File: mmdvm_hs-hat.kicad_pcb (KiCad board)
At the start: 2 copper layers, 65.1 x 30.2 mm, 82 parts, among them P1 I2C, P2 DISPLAY, P3 SMA, P4 STLINK, SW1 DNI, U1 ADF7021, U2 STM32F103C8T6, X1 TCXO, Y1 8MHz

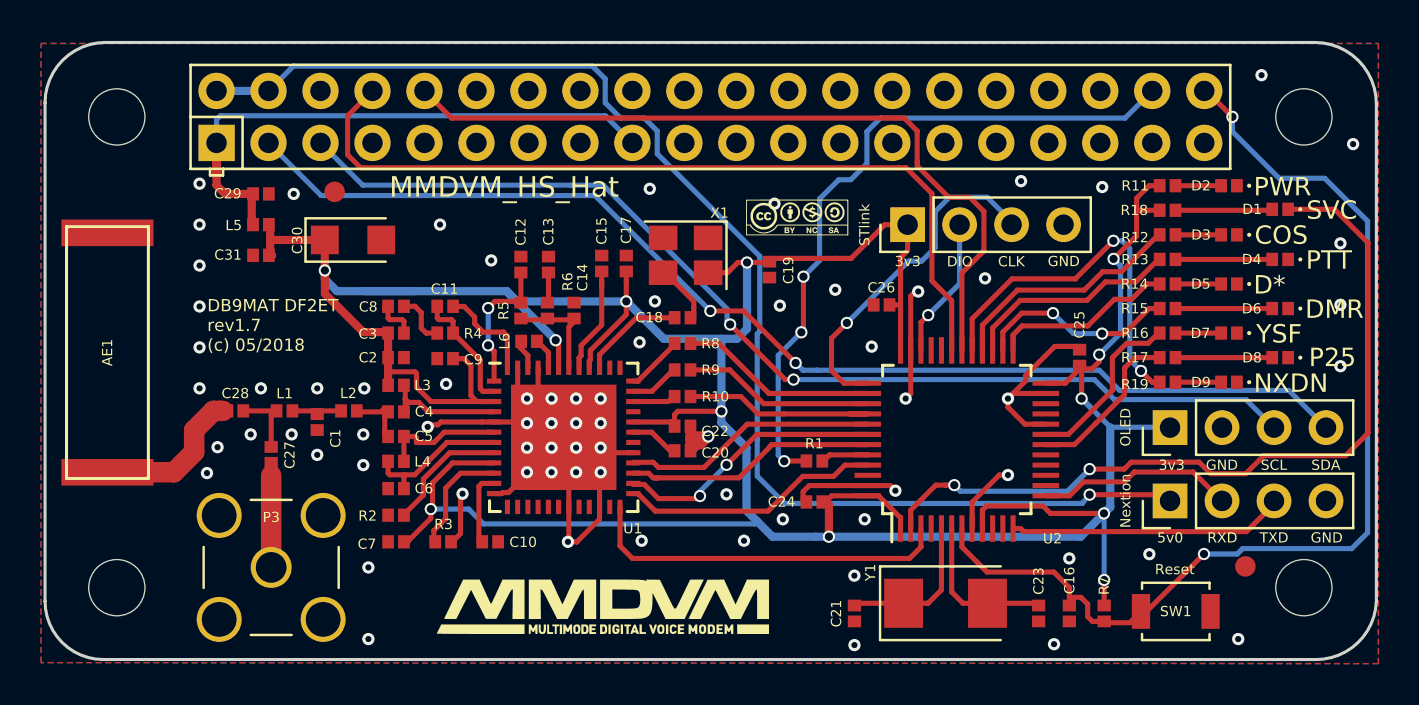
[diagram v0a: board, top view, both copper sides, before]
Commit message: Few track re-routed, few components moved. SMA sligthly moved to get better GND one for corners. Center tracks in 2x20 connector.
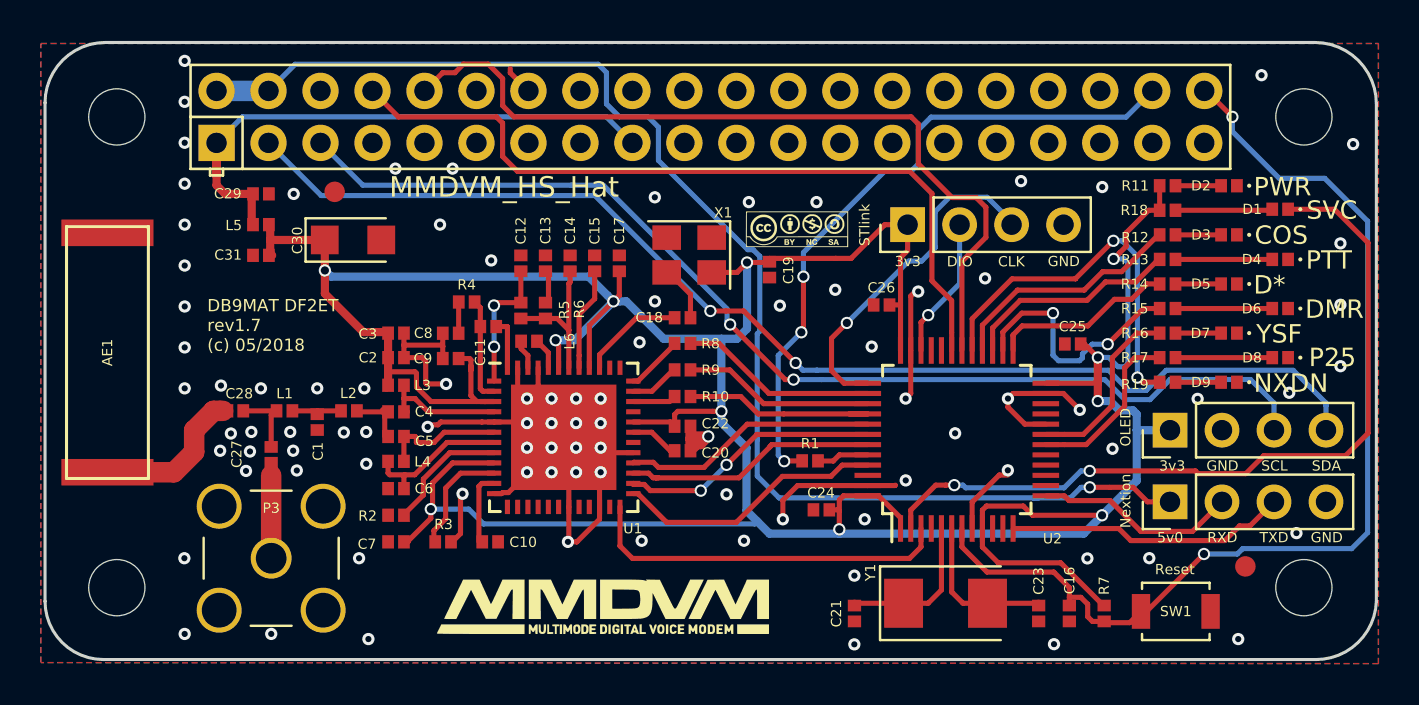
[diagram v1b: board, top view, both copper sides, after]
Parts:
- moved C8 2.98 mm to (175.3, 119.8)
- moved C11 2.33 mm to (177.1, 119.5)
- moved C14 2.32 mm to (181.1, 116.4)
- moved R4 1.85 mm to (176.1, 118.3)
- moved C25 0.75 mm to (205.7, 120.3), turned to 180 degrees
- moved G*** 0.57 mm to (192.2, 114.7)
- moved C24 0.52 mm to (193.4, 128.4)
- moved P3 0.45 mm to (166.5, 130.8)
- moved C15 0.34 mm to (182.3, 116.4)
- moved C17 0.34 mm to (183.5, 116.4)
- moved C9 0.27 mm to (175.3, 121.0)
- moved R1 0.21 mm to (192.8, 126.0)
- moved X1 0.17 mm to (186.9, 116.0)
- moved C13 0.16 mm to (179.9, 116.4)
- moved P1 0.13 mm to (210.4, 124.5)
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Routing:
- net GND: track 50.5 -> 56.2 mm, vias 73 -> 93
- net RXD: track 41.0 -> 38.4 mm
- net DMR_LED: track 9.80 -> 12.3 mm
- net Net-(C11-Pad1): track 5.00 -> 2.55 mm
- net Net-(C14-Pad1): track 4.99 -> 7.32 mm
- net TXD: track 38.0 -> 40.3 mm
- net SDA: track 57.5 -> 59.1 mm
- net SCL: track 52.7 -> 54.4 mm
- net VDD: track 178.7 -> 180.0 mm, vias 12 -> 11
- net Net-(PI1-Pad38): track 34.2 -> 33.0 mm
- net Net-(C8-Pad1): track 2.61 -> 1.53 mm
- net Net-(C11-Pad2): track 6.01 -> 5.08 mm
- net +5V: track 64.1 -> 65.0 mm
- net +3V3: track 29.1 -> 28.4 mm

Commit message: Add I2C OLED on 2x20 connector (should make it optional).
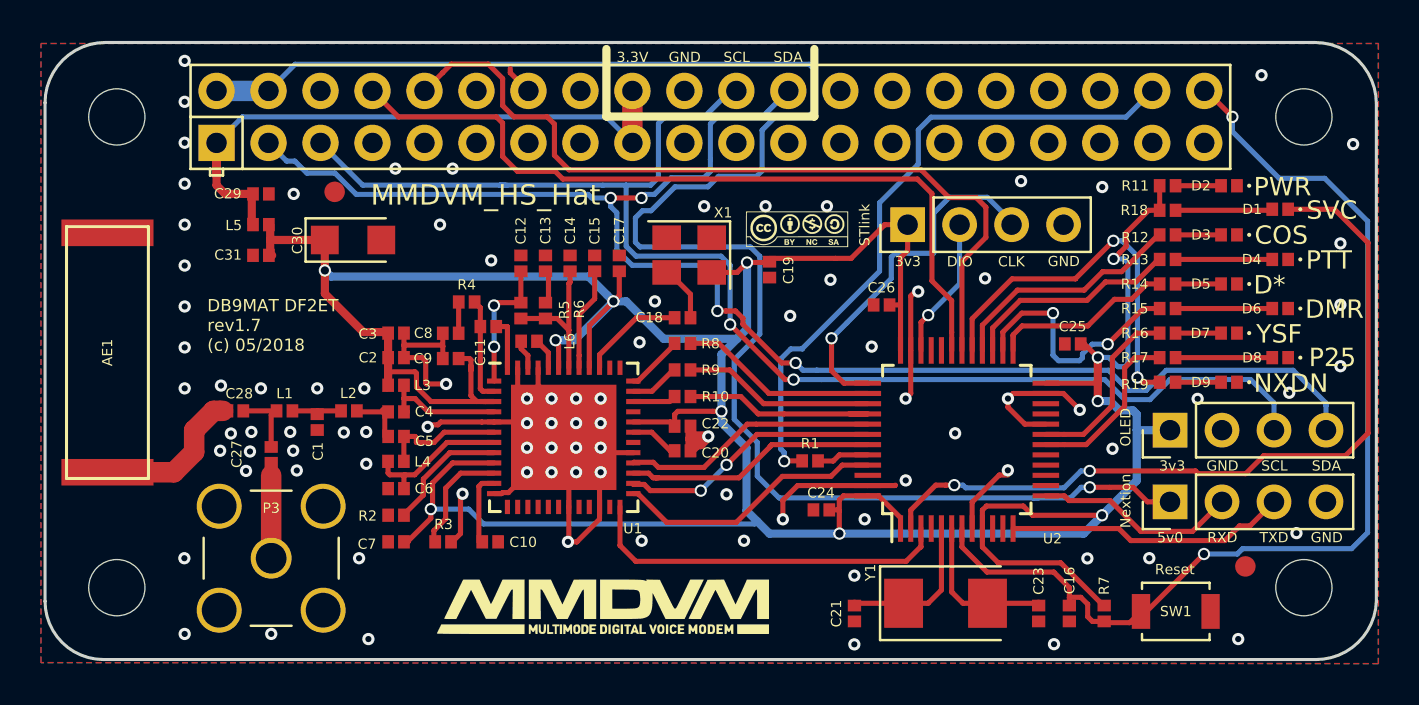
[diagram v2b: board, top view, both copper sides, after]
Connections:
- PI1 pad 18: Net-(PI1-Pad18) -> +3V3
- PI1 pad 22: Net-(PI1-Pad22) -> SCL
- PI1 pad 24: Net-(PI1-Pad24) -> SDA
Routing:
- net +5V: track 65.0 -> 84.6 mm
- net SDA: track 59.1 -> 73.9 mm, vias 2 -> 4
- net SCL: track 54.4 -> 66.6 mm
- net +3V3: track 28.4 -> 30.9 mm
- net SWCLK: track 16.9 -> 17.7 mm
- net Net-(PI1-Pad38): track 33.0 -> 32.5 mm, vias 3 -> 1
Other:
- board text added: "3.3V"

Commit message: Make OLED_on_2x20 optionnal, electrically (using 3x0402 unpopulated resistors).
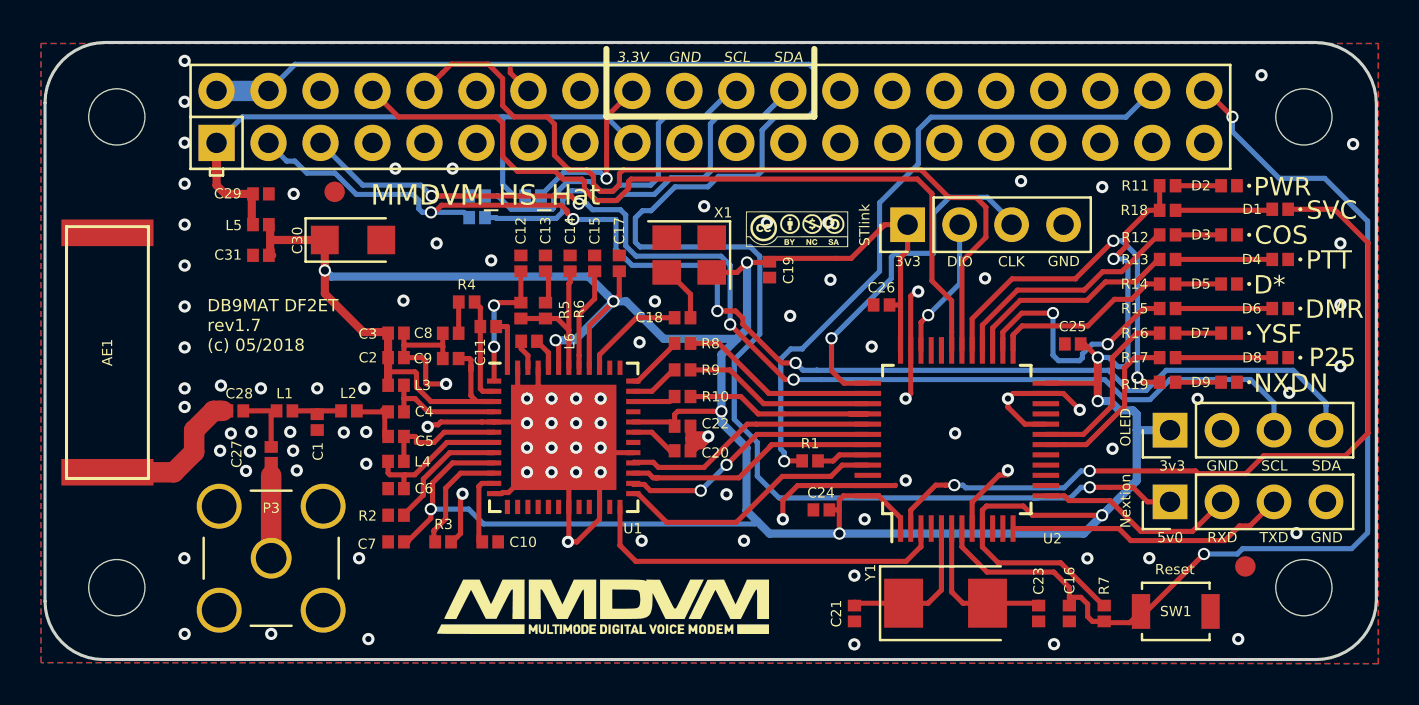
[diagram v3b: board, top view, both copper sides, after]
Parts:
- added R20: DNI, Resistor_SMD:R_0402_1005Metric, B.Cu at (179.3, 113.1)
- added R21: DNI, Resistor_SMD:R_0402_1005Metric, B.Cu at (176.6, 113.1)
- added R22: DNI, Resistor_SMD:R_0402_1005Metric, B.Cu at (176.6, 114.2)
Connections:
- PI1 pad 18: +3V3 -> Net-(PI1-Pad18)
- PI1 pad 22: SCL -> Net-(PI1-Pad22)
- PI1 pad 24: SDA -> Net-(PI1-Pad24)
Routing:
- net Net-(PI1-Pad24): track 0.00 -> 19.5 mm
- net Net-(PI1-Pad22): track 0.00 -> 17.3 mm
- net SDA: track 73.9 -> 63.9 mm
- net Net-(PI1-Pad18): track 0.00 -> 8.63 mm, vias 0 -> 1
- net SCL: track 66.6 -> 58.4 mm, vias 2 -> 4
- net +3V3: track 30.9 -> 33.0 mm
- net TXD: track 40.0 -> 41.4 mm
- net RXD: track 38.4 -> 39.7 mm
- net GND: vias 93 -> 95

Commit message: Fine tunning some tracks.
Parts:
- moved ? 0.30 mm to (214.0, 130.9)
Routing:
- net +5V: track 84.6 -> 79.8 mm
- net SDA: track 63.9 -> 64.9 mm
- net SCL: track 58.4 -> 59.1 mm
- net Net-(PI1-Pad38): track 32.5 -> 33.2 mm
- net SERVICE: track 38.9 -> 39.4 mm
- net GND: track 56.2 -> 56.0 mm, vias 95 -> 110

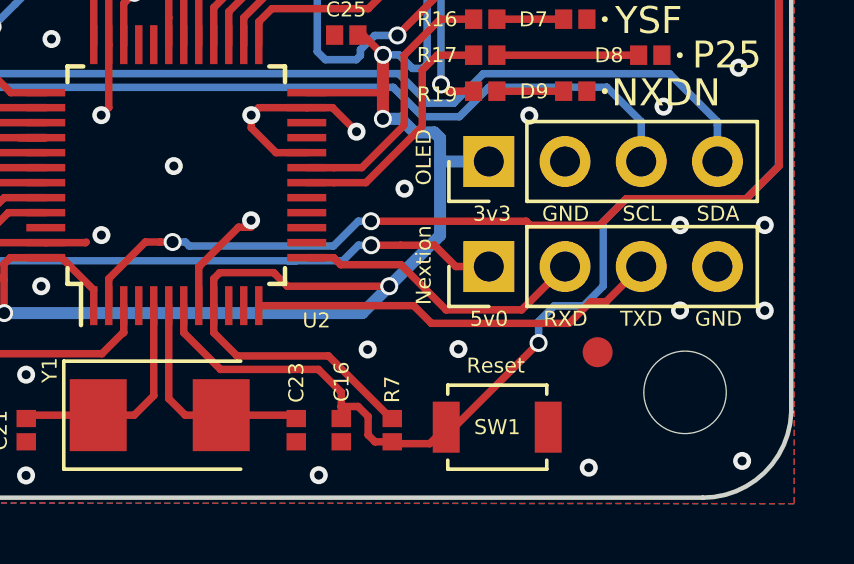
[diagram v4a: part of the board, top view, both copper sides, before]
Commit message: Fix DRC's fiducial warning.
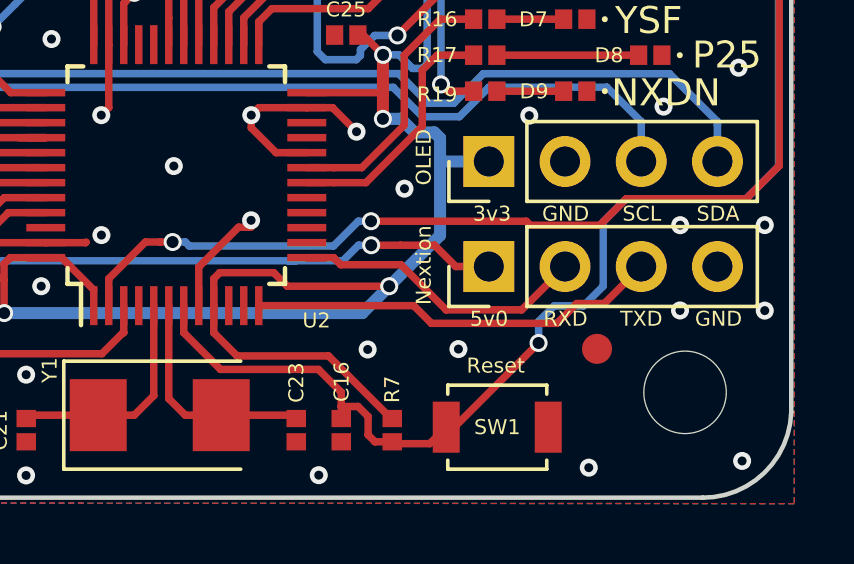
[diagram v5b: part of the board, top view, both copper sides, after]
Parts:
- moved ? 0.11 mm to (214.0, 130.8)
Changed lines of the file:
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@@
-(kicad_pcb (version 20171130) (host pcbnew 5.0.0-rc2-unknown-dfa9175~65~ubuntu16.04.1)
+(kicad_pcb (version 20171130) (host pcbnew 5.0.0-rc2-unknown-fc71fc6~65~ubuntu16.04.1)
   (general
     (thickness 1.6)
@@
     (0 F.Cu signal)
     (31 B.Cu signal)
-    (32 B.Adhes user hide)
-    (33 F.Adhes user hide)
+    (32 B.Adhes user)
+    (33 F.Adhes user)
     (34 B.Paste user)
-    (35 F.Paste user hide)
-    (36 B.SilkS user hide)
-    (37 F.SilkS user hide)
+    (35 F.Paste user)
+    (36 B.SilkS user)
+    (37 F.SilkS user)
     (38 B.Mask user)
-    (39 F.Mask user hide)
-    (40 Dwgs.User user hide)
-    (41 Cmts.User user hide)
-    (42 Eco1.User user hide)
-    (43 Eco2.User user hide)
+    (39 F.Mask user)
+    (40 Dwgs.User user)
+    (41 Cmts.User user)
+    (42 Eco1.User user)
+    (43 Eco2.User user)
     (44 Edge.Cuts user)
-    (45 Margin user hide)
+    (45 Margin user)
     (46 B.CrtYd user)
-    (47 F.CrtYd user hide)
+    (47 F.CrtYd user)
     (48 B.Fab user)
-    (49 F.Fab user hide)
+    (49 F.Fab user)
   )
   (setup
@@
   )
   (module Fiducial:Fiducial_1mm_Dia_2.54mm_Outer_CopperTop locked (layer F.Cu)
-    (at 214.0458 130.90144)
+    (at 214.02548 130.78968)
     (descr "Circular Fiducial, 1mm bare copper top; 2.54mm keepout")
     (tags marker)
@@
   (segment (start 180.3781 111.8997) (end 180.75191 112.27351) (width 0.25) (layer F.Cu) (net 18))
   (segment (start 215.5 128) (end 215.5 128.1524) (width 0.25) (layer F.Cu) (net 19))
-  (segment (start 214.323679 129.220721) (end 215.49868 128.04572) (width 0.25) (layer F.Cu) (net 19))
-  (segment (start 213.813899 129.220721) (end 214.323679 129.220721) (width 0.25) (layer F.Cu) (net 19))
-  (segment (start 202.75 129.35) (end 207.91474 129.35) (width 0.25) (layer F.Cu) (net 19))
-  (segment (start 207.91474 129.35) (end 208.50395 129.93921) (width 0.25) (layer F.Cu) (net 19))
-  (segment (start 208.50395 129.93921) (end 213.09541 129.93921) (width 0.25) (layer F.Cu) (net 19))
-  (segment (start 213.09541 129.93921) (end 213.813899 129.220721) (width 0.25) (layer F.Cu) (net 19))
+  (segment (start 207.91474 129.35) (end 202.75 129.35) (width 0.25) (layer F.Cu) (net 19))
+  (segment (start 215.49868 128.04572) (end 214.26602 129.27838) (width 0.25) (layer F.Cu) (net 19))
+  (segment (start 208.50395 129.93921) (end 207.91474 129.35) (width 0.25) (layer F.Cu) (net 19))
+  (segment (start 213.34984 129.27838) (end 212.68901 129.93921) (width 0.25) (layer F.Cu) (net 19))
+  (segment (start 214.26602 129.27838) (end 213.34984 129.27838) (width 0.25) (layer F.Cu) (net 19))
+  (segment (start 212.68901 129.93921) (end 208.50395 129.93921) (width 0.25) (layer F.Cu) (net 19))
   (segment (start 205.484999 127.984999) (end 207.490001 127.984999) (width 0.25) (layer F.Cu) (net 20))
   (segment (start 205.25 127.75) (end 205.484999 127.984999) (width 0.25) (layer F.Cu) (net 20))

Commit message: Last silkscreen changes for this release.
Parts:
- moved G*** 14.5 mm to (177.8, 113.0)
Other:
- board text added: "DB9MAT DF2ET F1RMB"
- board text added: "rev1.7 (c) 06/2018"
- board text removed: "DB9MAT DF2ET rev1.7 (c) 05/2018"
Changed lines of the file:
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@@
   (general
     (thickness 1.6)
-    (drawings 52)
+    (drawings 61)
     (tracks 912)
     (zones 0)
@@
     (40 Dwgs.User user)
     (41 Cmts.User user)
-    (42 Eco1.User user)
-    (43 Eco2.User user)
+    (42 Eco1.User user hide)
+    (43 Eco2.User user hide)
     (44 Edge.Cuts user)
     (45 Margin user)
-    (46 B.CrtYd user)
-    (47 F.CrtYd user)
-    (48 B.Fab user)
-    (49 F.Fab user)
+    (46 B.CrtYd user hide)
+    (47 F.CrtYd user hide)
+    (48 B.Fab user hide)
+    (49 F.Fab user hide)
   )
   (setup
@@
     (zone_45_only yes)
     (trace_min 0.2)
-    (segment_width 0.01)
+    (segment_width 0.3)
     (edge_width 0.15)
     (via_size 0.6)
@@
   )
   (module Logos:Logo_silk_CC-BY-NC-SA_5x2mm locked (layer F.Cu)
-    (at 192.19418 114.72418)
+    (at 177.76698 112.99444)
     (descr "CC BY-NC-SA logo, 5x2mm")
     (fp_text reference G*** (at 0.2 -0.7) (layer F.SilkS) hide
@@
       (xy 2.4765 -0.87122) (xy 2.49936 -0.86868) (xy 2.49936 0.00254) (xy 2.49936 0.87376)) (layer F.SilkS) (width 0.00254))
   )
+  (gr_line (start 213.36 106.697567) (end 213.36 109.242861) (layer F.SilkS) (width 0.3))
+  (gr_line (start 208.28254 106.69778) (end 213.36 106.69778) (layer F.SilkS) (width 0.3))
+  (gr_line (start 162.56508 111.77524) (end 162.56508 106.7181) (layer F.SilkS) (width 0.3))
+  (gr_line (start 175.262542 111.77524) (end 162.56508 111.77524) (layer F.SilkS) (width 0.3))
+  (gr_line (start 162.56508 106.7181) (end 175.262552 106.7181) (layer F.SilkS) (width 0.3))
+  (gr_line (start 208.28254 109.24286) (end 213.36 109.24286) (layer F.SilkS) (width 0.3))
+  (gr_line (start 208.28254 106.69778) (end 208.28254 109.24286) (layer F.SilkS) (width 0.3))
+  (gr_line (start 175.26254 106.7181) (end 175.26254 111.77524) (layer F.SilkS) (width 0.3))
+  (gr_text "rev1.7 \n(c) 06/2018" (at 163.3601 120.8405) (layer F.SilkS)
+    (effects (font (size 0.6 0.6) (thickness 0.15)) (justify left))
+  )
   (gr_line (start 175.2219 115.1382) (end 175.2219 112.22736) (layer B.SilkS) (width 0.3))
   (gr_line (start 180.662585 115.1382) (end 175.2219 115.1382) (layer B.SilkS) (width 0.3))
@@
   )
   (target plus (at 169.6 112.9) (size 5) (width 0.15) (layer Edge.Cuts))
-  (gr_text NXDN (at 216.32418 122.25528) (layer F.SilkS)
-    (effects (font (size 0.9 0.9) (thickness 0.225)))
+  (gr_text NXDN (at 215.93302 122.24258) (layer F.SilkS)
+    (effects (font (size 0.7 0.7) (thickness 0.175)))
   )
   (gr_text 3v3 (at 197.60692 116.29644) (layer F.SilkS)
@@
     (effects (font (size 0.5 0.5) (thickness 0.125)))
   )
-  (gr_text SVC (at 218.32316 113.79708) (layer F.SilkS)
-    (effects (font (size 0.9 0.9) (thickness 0.225)))
+  (gr_text SVC (at 218.0463 113.78946) (layer F.SilkS)
+    (effects (font (size 0.7 0.7) (thickness 0.175)))
   )
   (gr_line (start 158.4 105.6) (end 217.5 105.6) (layer Edge.Cuts) (width 0.15))
@@
   (gr_arc (start 158.3 132.9) (end 158.3 135.75) (angle 90) (layer Edge.Cuts) (width 0.15))
   (gr_arc (start 158.4 108.55) (end 155.45 108.55) (angle 90) (layer Edge.Cuts) (width 0.15))
-  (gr_text "DB9MAT DF2ET\nrev1.7 \n(c) 05/2018" (at 163.37534 119.42318) (layer F.SilkS)
+  (gr_text "DB9MAT DF2ET F1RMB" (at 163.3601 118.86184) (layer F.SilkS)
     (effects (font (size 0.6 0.6) (thickness 0.15)) (justify left))
   )
-  (gr_text MMDVM_HS_Hat (at 171.35856 113.06048) (layer F.SilkS)
+  (gr_text MMDVM_HS_Hat (at 163.28644 117.37848) (layer F.SilkS)
     (effects (font (size 1 1) (thickness 0.25)) (justify left))
   )
@@
     (effects (font (size 0.5 0.5) (thickness 0.125)))
   )
-  (gr_text YSF (at 215.7476 119.84482) (layer F.SilkS)
-    (effects (font (size 0.9 0.9) (thickness 0.225)))
+  (gr_text YSF (at 215.52916 119.83466) (layer F.SilkS)
+    (effects (font (size 0.7 0.7) (thickness 0.175)))
   )
-  (gr_text P25 (at 218.35364 120.99544) (layer F.SilkS)
-    (effects (font (size 0.9 0.9) (thickness 0.225)))
+  (gr_text P25 (at 218.080573 121.0437) (layer F.SilkS)
+    (effects (font (size 0.7 0.7) (thickness 0.175)))
   )
-  (gr_text DMR (at 218.4527 118.63832) (layer F.SilkS)
-    (effects (font (size 0.9 0.9) (thickness 0.225)))
+  (gr_text DMR (at 218.16822 118.63578) (layer F.SilkS)
+    (effects (font (size 0.7 0.7) (thickness 0.175)))
   )
-  (gr_text D* (at 215.28024 117.4496) (layer F.SilkS)
-    (effects (font (size 0.9 0.9) (thickness 0.225)))
+  (gr_text D* (at 215.14054 117.43182) (layer F.SilkS)
+    (effects (font (size 0.7 0.7) (thickness 0.175)))
   )
-  (gr_text PTT (at 218.17838 116.23548) (layer F.SilkS)
-    (effects (font (size 0.9 0.9) (thickness 0.225)))
+  (gr_text PTT (at 217.95232 116.2431) (layer F.SilkS)
+    (effects (font (size 0.7 0.7) (thickness 0.175)))
   )
-  (gr_text COS (at 215.85428 115.02136) (layer F.SilkS)
-    (effects (font (size 0.9 0.9) (thickness 0.225)))
+  (gr_text COS (at 215.56726 115.03406) (layer F.SilkS)
+    (effects (font (size 0.7 0.7) (thickness 0.175)))
   )
-  (gr_text PWR (at 215.91524 112.65408) (layer F.SilkS)
-    (effects (font (size 0.9 0.9) (thickness 0.225)))
+  (gr_text PWR (at 215.62314 112.64392) (layer F.SilkS)
+    (effects (font (size 0.7 0.7) (thickness 0.175)))
   )
   (segment (start 181.04375 128.29375) (end 181.04375 127.21875) (width 0.25) (layer F.Cu) (net 1))
